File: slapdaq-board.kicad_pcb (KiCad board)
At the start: 4 copper layers, 96.2 x 145.8 mm, 72 parts, among them J1 Higher Screw Terminals, J2 Lower Screw Terminals, J3 USB-C, Q1 BSS84, U1 LM2675M-3.3, U2 LM2675M-5, U3 ESP32-S3, U4 DT1042-04SO-7, U5 REF3333, U6 ADS1261, U7 MAX31856

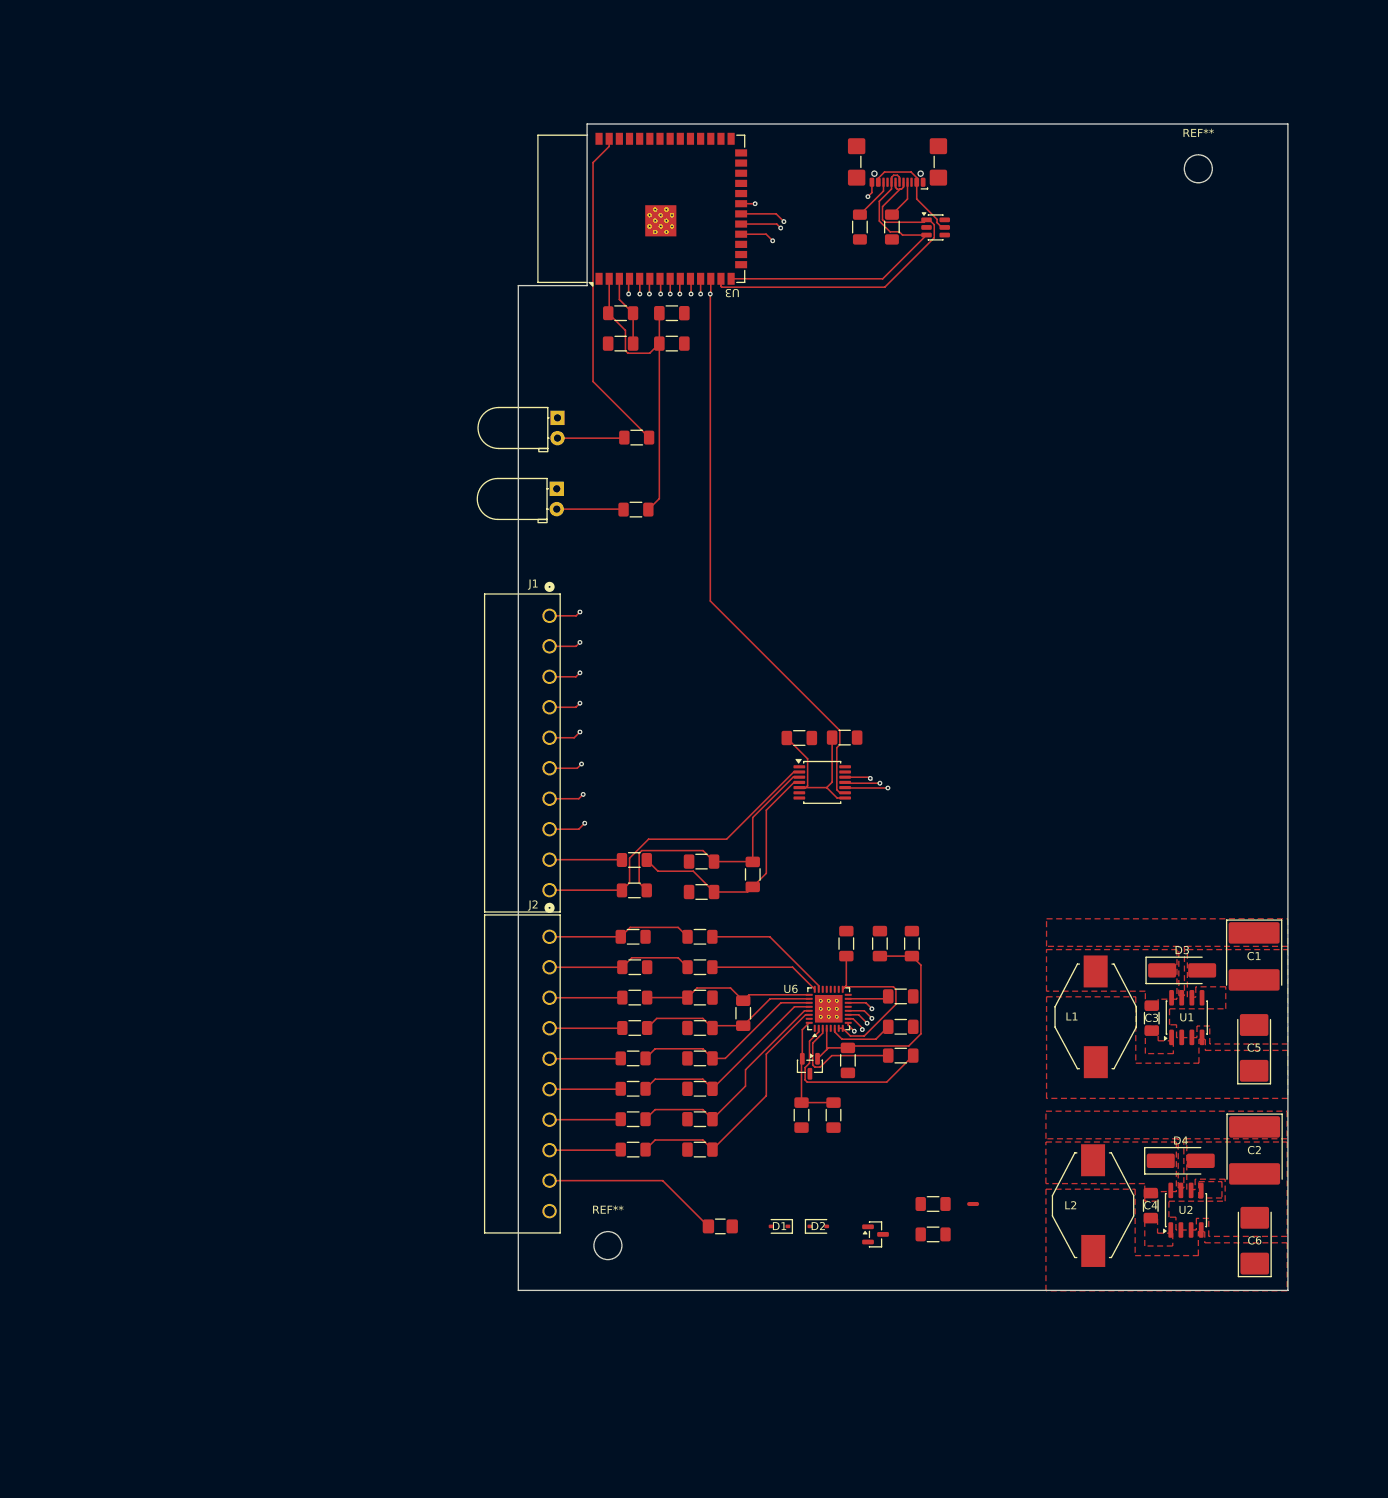
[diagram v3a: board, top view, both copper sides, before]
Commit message: Finalize board outline
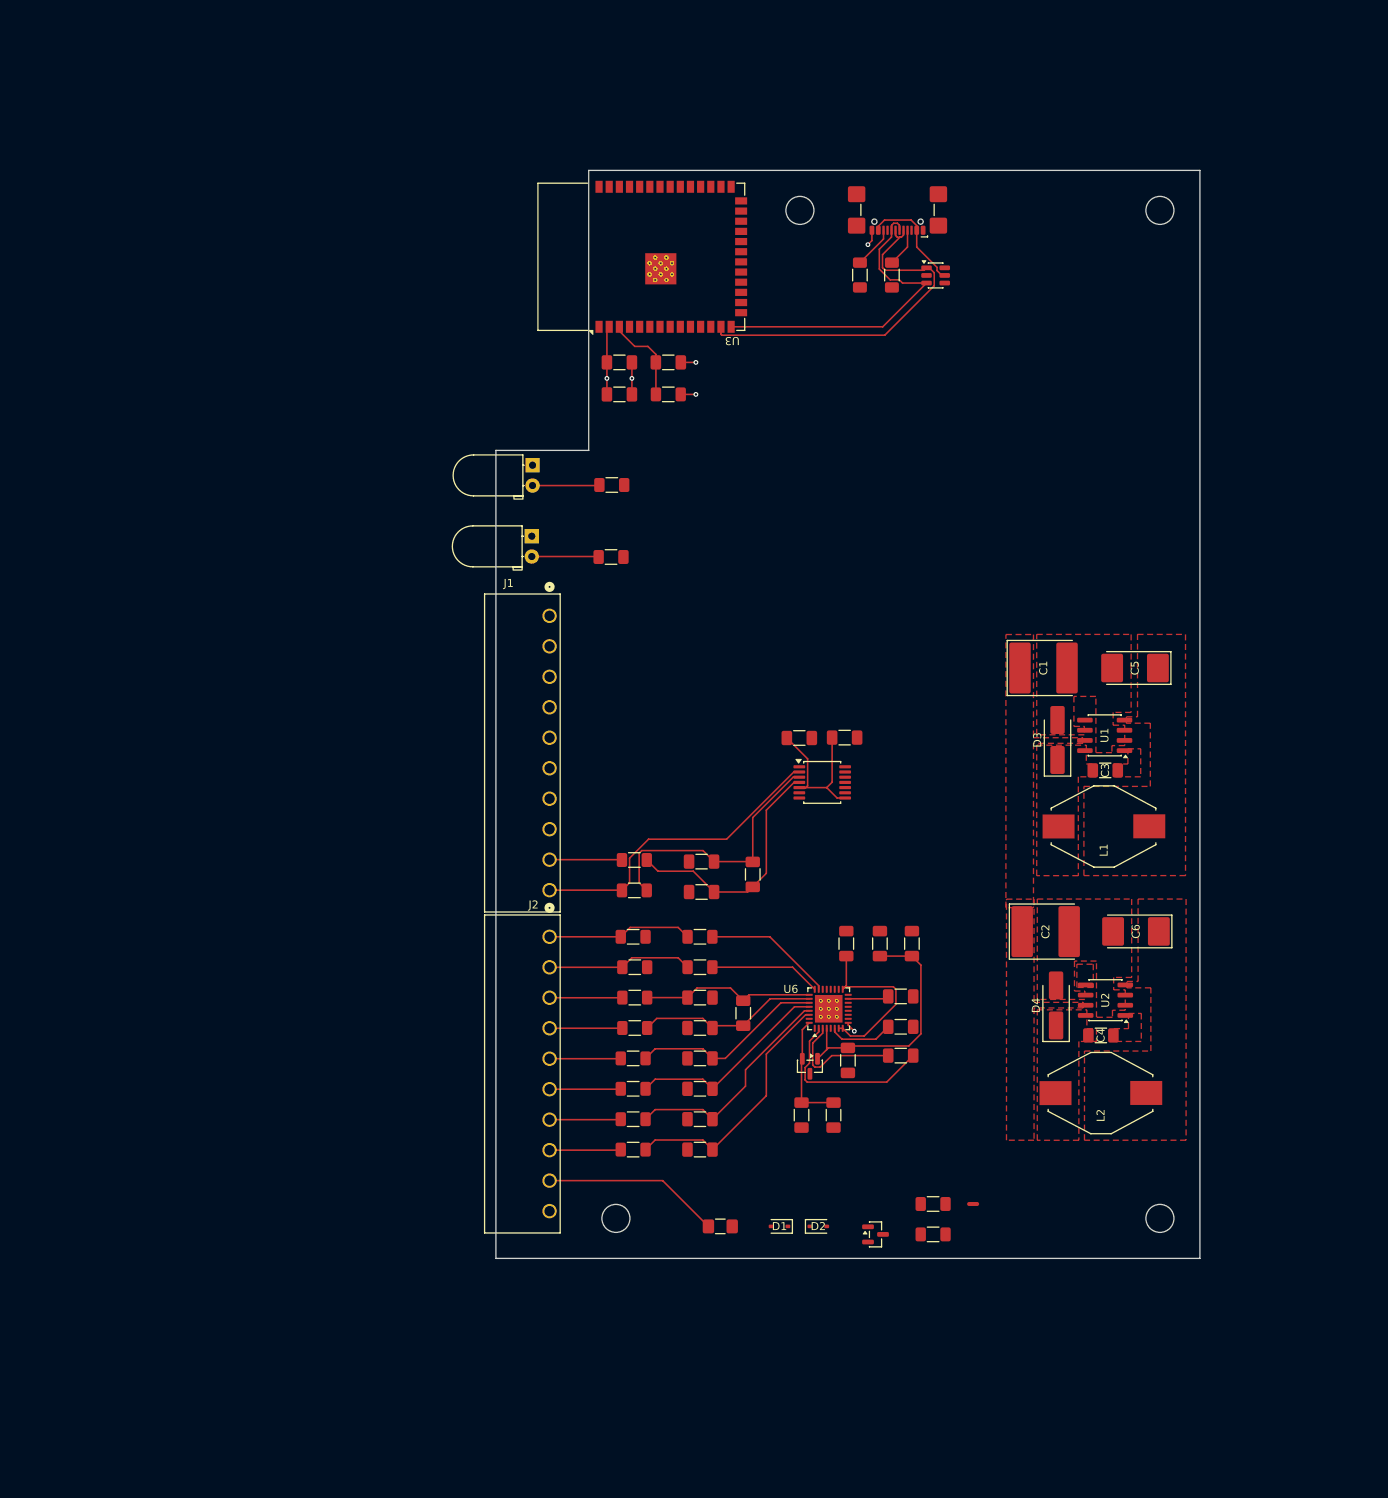
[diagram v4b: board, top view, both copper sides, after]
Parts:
- added REF**: MountingHole_3.5mm, MountingHole:MountingHole_3.5mm, F.Cu at (133.0, 61.0)
- added REF**: MountingHole_3.5mm, MountingHole:MountingHole_3.5mm, F.Cu at (178.0, 187.0)
- moved C5 49.8 mm to (174.9, 118.2), turned to 180 degrees
- moved C1 44.6 mm to (163.4, 118.2), turned to 0 degrees
- moved C6 41.4 mm to (175.0, 151.1), turned to 180 degrees
- moved C2 37.8 mm to (163.7, 151.2), turned to 0 degrees
- moved U1 36.7 mm to (171.1, 126.6), turned to 180 degrees
- moved D3 32.7 mm to (165.2, 127.2), turned to 90 degrees
- moved C3 31.5 mm to (171.2, 131.0), turned to 180 degrees
- moved U2 28.1 mm to (171.2, 159.7), turned to 180 degrees
- moved D4 24.9 mm to (165.0, 160.4), turned to 90 degrees
- moved L1 23.8 mm to (171.0, 138.0), turned to 180 degrees
- moved C4 22.2 mm to (170.6, 164.1), turned to 180 degrees
- moved L2 14.1 mm to (170.6, 171.3), turned to 180 degrees
- moved R3 11.8 mm to (116.5, 84.0), turned to 180 degrees
- moved C9 9.12 mm to (110.4, 84.0)
- moved C8 8.99 mm to (110.4, 80.0)
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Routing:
- net SPI_CLK: track 121.1 -> 0.00 mm, vias 3 -> 0
- net SPI_D: track 117.4 -> 0.00 mm, vias 3 -> 0
- net SPI_Q: track 114.9 -> 0.00 mm, vias 3 -> 0
- net CS0_ADC: track 110.0 -> 0.00 mm, vias 2 -> 0
- net DIO7: track 78.8 -> 0.00 mm, vias 2 -> 0
- net DIO6: track 74.5 -> 0.00 mm, vias 2 -> 0
- net CS1_THR: track 72.0 -> 0.00 mm, vias 1 -> 0
- net DIO5: track 70.0 -> 0.00 mm, vias 2 -> 0
- net DIO4: track 65.4 -> 0.00 mm, vias 2 -> 0
- net DIO3: track 61.3 -> 0.00 mm, vias 2 -> 0
- net DIO2: track 56.9 -> 0.00 mm, vias 2 -> 0
- net DIO1: track 52.6 -> 0.00 mm, vias 2 -> 0
- net DIO0: track 48.2 -> 0.00 mm, vias 2 -> 0
- net /MCU/WIFI_LED: track 41.1 -> 0.00 mm
- net +3.3V: track 83.2 -> 53.8 mm, vias 0 -> 2
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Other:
- board size 96.2 x 145.8 mm -> 88 x 136 mm

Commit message: Add ground and power planes
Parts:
- moved C19 8.69 mm to (131.0, 168.0), turned to 90 degrees
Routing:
- net +3.3V: track 53.8 -> 36.3 mm
- net GND: track 9.26 -> 18.6 mm, vias 4 -> 7
- net Net-(U5-OUT): track 14.4 -> 10.4 mm
- added copper zone on In2.Cu, net +3.3V
- added copper zone on In1.Cu, net GND
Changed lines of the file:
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@@
 	(footprint "Capacitor_SMD:C_1206_3216Metric_Pad1.33x1.80mm_HandSolder"
 		(layer "F.Cu")
-		(at 137.2 174.0875 -90)
+		(at 131 168 90)
 		(descr "Capacitor SMD 1206 (3216 Metric), square (rectangular) end terminal, IPC-7351 nominal with elongated pad for handsoldering. (Body size source: IPC-SM-782 page 76, https://www.pcb-3d.com/wordpress/wp-content/uploads/ipc-sm-782a_amendment_1_and_2.pdf)")
 		(tags "capacitor handsolder")
 		(property "Reference" "C19"
-			(at 0 -1.85 90)
+			(at 3 0 0)
 			(layer "F.SilkS")
-			(hide yes)
 			(effects
 				(font
@@
 		)
 		(property "Mouser Link" "https://www.mouser.com/en/ProductDetail/Murata-Electronics/GRM31CR72E104KW03L?qs=dSG6KG9Gilq13HemRFxTRg%3D%3D"
-			(at 0 0 270)
+			(at 0 0 90)
 			(unlocked yes)
 			(layer "F.Fab")
@@
 		)
 		(property "MPN" "GRM31CR72E104KW03L"
-			(at 0 0 270)
+			(at 0 0 90)
 			(unlocked yes)
 			(layer "F.Fab")
@@
 		(duplicate_pad_numbers_are_jumpers no)
 		(fp_line
-			(start -0.711252 0.91)
-			(end 0.711252 0.91)
+			(start -0.711252 -0.91)
+			(end 0.711252 -0.91)
 			(stroke
 				(width 0.12)
@@
 		)
 		(fp_line
-			(start -0.711252 -0.91)
-			(end 0.711252 -0.91)
+			(start -0.711252 0.91)
+			(end 0.711252 0.91)
 			(stroke
 				(width 0.12)
@@
 		)
 		(pad "1" smd roundrect
-			(at -1.5625 0 270)
+			(at -1.5625 0 90)
 			(size 1.325 1.8)
 			(layers "F.Cu" "F.Mask" "F.Paste")
@@
 		)
 		(pad "2" smd roundrect
-			(at 1.5625 0 270)
+			(at 1.5625 0 90)
 			(size 1.325 1.8)
 			(layers "F.Cu" "F.Mask" "F.Paste")
@@
 		(tags "capacitor handsolder")
 		(property "Reference" "C18"
-			(at 0 -1.85 90)
+			(at -0.037252 -2.625372 180)
 			(layer "F.SilkS")
-			(hide yes)
 			(effects
 				(font
@@
 	)
 	(segment
-		(start 142 63.48)
-		(end 142 64.78)
+		(start 148.4 64.4)
+		(end 149 65)
 		(width 0.2)
 		(layer "F.Cu")
@@
 	)
 	(segment
+		(start 140.09 61)
+		(end 140.09 62.905)
+		(width 0.2)
+		(layer "F.Cu")
+		(net "GND")
+	)
+	(segment
+		(start 150.31 61)
+		(end 150.31 62.905)
+		(width 0.2)
+		(layer "F.Cu")
+		(net "GND")
+	)
+	(segment
 		(start 139.0375 162.8375)
 		(end 139.8 163.6)
@@
 	)
 	(segment
-		(start 142 64.78)
-		(end 141.5 65.28)
+		(start 148.4 63.48)
+		(end 148.4 64.4)
 		(width 0.2)
 		(layer "F.Cu")
@@
 		(net "GND")
 	)
+	(segment
+		(start 142 64.5)
+		(end 142 63.48)
+		(width 0.2)
+		(layer "F.Cu")
+		(net "GND")
+	)
+	(segment
+		(start 141.5 65)
+		(end 142 64.5)
+		(width 0.2)
+		(layer "F.Cu")
+		(net "GND")
+	)
+	(segment
+		(start 140.09 58.975)
+		(end 140.09 61)
+		(width 0.2)
+		(layer "F.Cu")
+		(net "GND")
+	)
+	(segment
+		(start 150.31 58.975)
+		(end 150.31 61)
+		(width 0.2)
+		(layer "F.Cu")
+		(net "GND")
+	)
 	(via
 		(at 120 80)
@@
 	)
 	(via
+		(at 149 65)
+		(size 0.6)
+		(drill 0.3)
+		(layers "F.Cu" "B.Cu")
+		(net "GND")
+	)
+	(via
 		(at 112 82)
 		(size 0.6)
@@
 	)
 	(via
-		(at 141.5 65.28)
+		(at 141.5 65)
+		(size 0.6)
+		(drill 0.3)
+		(layers "F.Cu" "B.Cu")
+		(net "GND")
+	)
+	(via
+		(at 150.31 61)
+		(size 0.6)
+		(drill 0.3)
+		(layers "F.Cu" "B.Cu")
+		(net "GND")
+	)
+	(via
+		(at 140.09 61)
 		(size 0.6)
 		(drill 0.3)
@@
 	)
 	(segment
-		(start 145 160.240256)
-		(end 141.040256 164.2)
-		(width 0.2)
-		(layer "F.Cu")
-		(net "+3.3V")
-	)
-	(segment
 		(start 108.875 84)
 		(end 108.875 82)
@@
 	)
 	(segment
-		(start 138.6625 158.05)
-		(end 144.684744 158.05)
-		(width 0.2)
-		(layer "F.Cu")
-		(net "+3.3V")
-	)
-	(segment
 		(start 137.025 126.9)
 		(end 137.025 132.475)
@@
 	)
 	(segment
-		(start 145 158.365256)
-		(end 145 160.240256)
-		(width 0.2)
-		(layer "F.Cu")
-		(net "+3.3V")
-	)
-	(segment
 		(start 108.875 75.835)
 		(end 109.16 75.55)
@@
 	)
 	(segment
-		(start 139.3125 164.2)
-		(end 138.35 163.2375)
-		(width 0.2)
-		(layer "F.Cu")
-		(net "+3.3V")
-	)
-	(segment
-		(start 141.040256 164.2)
-		(end 139.3125 164.2)
-		(width 0.2)
-		(layer "F.Cu")
-		(net "+3.3V")
-	)
-	(segment
-		(start 144.684744 158.05)
-		(end 145 158.365256)
-		(width 0.2)
-		(layer "F.Cu")
-		(net "+3.3V")
-	)
-	(segment
-		(start 138.35 158.3625)
-		(end 138.6625 158.05)
-		(width 0.2)
-		(layer "F.Cu")
-		(net "+3.3V")
-	)
-	(segment
 		(start 138.8 154.2125)
 		(end 138.8 157.9125)
@@
 	)
 	(segment
-		(start 133.4 172.525)
-		(end 137.4 172.525)
-		(width 0.2)
-		(layer "F.Cu")
-		(net "Net-(U5-OUT)")
-	)
-	(segment
 		(start 133.3 167.05)
 		(end 133.3 163.4125)
@@
 			)
 		)
+	)
+	(zone
+		(net "GND")
+		(layer "In1.Cu")
+		(hatch edge 0.5)
+		(priority 6)
+		(connect_pads yes
+			(clearance 0.2)
+		)
+		(min_thickness 0.25)
+		(fill yes
+			(thermal_gap 0.5)
+			(thermal_bridge_width 0.5)
+			(island_removal_mode 0)
+		)
+		(polygon
+			(pts
+				(xy 93 54) (xy 185 54) (xy 185 194) (xy 93 194)
+			)
+		)
+	)
+	(zone
+		(net "+3.3V")
+		(layer "In2.Cu")
+		(hatch edge 0.5)
+		(priority 6)
+		(connect_pads yes
+			(clearance 0.2)
+		)
+		(min_thickness 0.25)
+		(fill yes
+			(thermal_gap 0.5)
+			(thermal_bridge_width 0.5)
+			(island_removal_mode 0)
+		)
+		(polygon
+			(pts
+				(xy 93 54) (xy 185 54) (xy 185 194) (xy 93 194)
+			)
+		)

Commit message: tracing
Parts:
- moved C21 21.9 mm to (140.6, 174.4), turned to 90 degrees
- moved C20 21.8 mm to (145.6, 174.4), turned to 90 degrees
- moved C17 8.01 mm to (135.4, 174.4)
- moved NT1 5.44 mm to (151.6, 180.7), turned to -90 degrees
- moved C18 2.62 mm to (130.6, 174.4)
- moved C9 1.20 mm to (110.4, 85.2)
- moved R3 1.20 mm to (116.5, 85.2)
- moved C19 0.89 mm to (130.6, 167.2)
- moved U5 0.50 mm to (134.8, 168.0)
- moved Q1 0.10 mm to (142.5, 188.9)
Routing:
- net Vbus: track 13.8 -> 138.9 mm
- net SPI_Q: track 0.00 -> 122.4 mm, vias 0 -> 3
- net SPI_CLK: track 0.00 -> 117.2 mm, vias 0 -> 3
- net SPI_D: track 0.00 -> 113.8 mm, vias 0 -> 3
- net CS0_ADC: track 0.00 -> 105.1 mm, vias 0 -> 2
- net GND: track 18.6 -> 113.8 mm, vias 7 -> 43
- net CS1_THR: track 0.00 -> 82.9 mm, vias 0 -> 3
- net DIO7: track 0.00 -> 73.8 mm, vias 0 -> 2
- net DIO6: track 0.00 -> 69.7 mm, vias 0 -> 2
- net DIO5: track 0.00 -> 65.3 mm, vias 0 -> 2
- net DIO4: track 0.00 -> 60.8 mm, vias 0 -> 2
- net DIO3: track 0.00 -> 56.3 mm, vias 0 -> 2
- net DIO2: track 0.00 -> 51.9 mm, vias 0 -> 2
- net DIO1: track 0.00 -> 47.6 mm, vias 0 -> 2
- net DIO0: track 0.00 -> 43.3 mm, vias 0 -> 2
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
